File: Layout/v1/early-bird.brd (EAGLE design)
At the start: 98.5 x 80.8 mm, 61 parts, among them J1 22-27-2021-02, J2 AVR_SPI_PRG_62X3_LOCK, U1 ATMEGA328P-AU

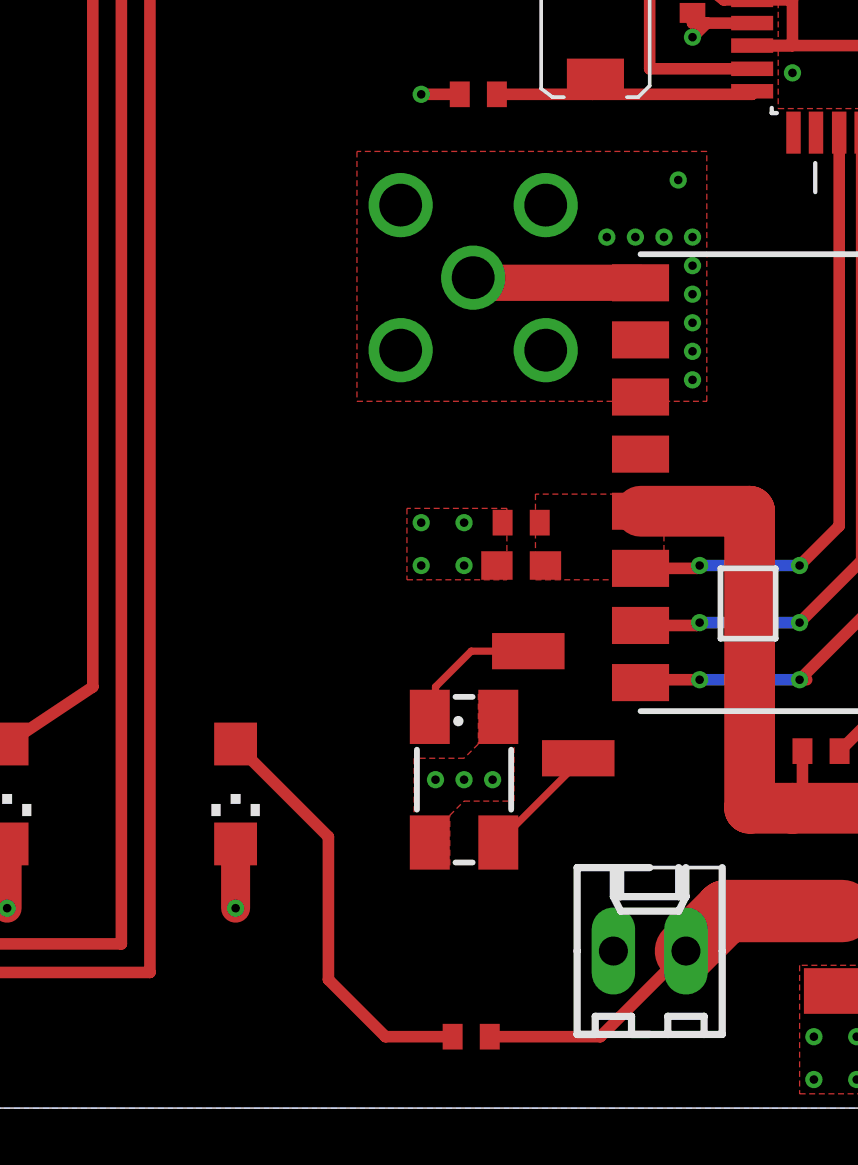
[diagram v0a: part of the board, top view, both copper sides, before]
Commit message: Update silkscreen.
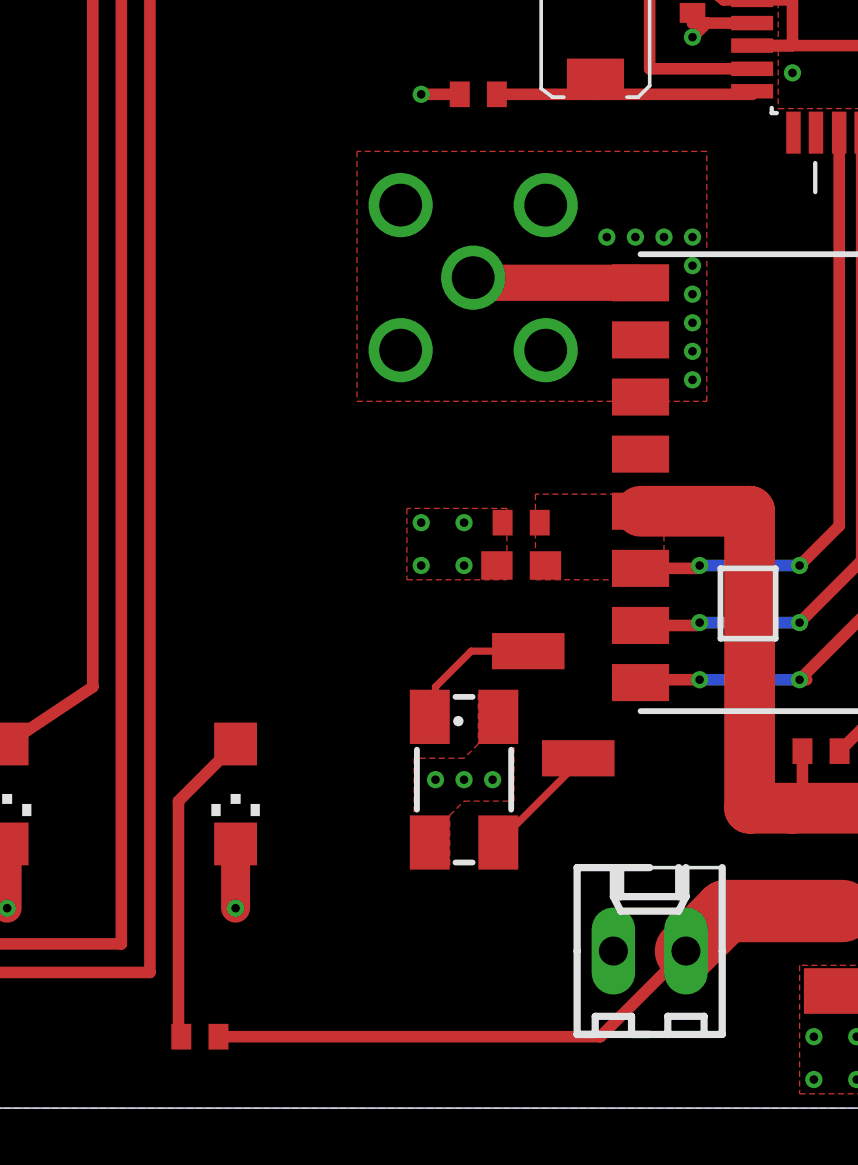
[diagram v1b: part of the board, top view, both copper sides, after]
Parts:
- moved R10 9.50 mm to (39.8, 2.50)
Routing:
- net AUX+: track 17.2 -> 26.7 mm
- net N$15: track 14.8 -> 11.2 mm
- net BATT-: vias 144 -> 143
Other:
- board text added: "10uH"
- board text added: "AA"
- board text added: "ATMega328"
- board text added: "AUX"
- board text added: "ENABLE AUX"
- board text added: "ICSP"
- board text added: "MAX-M8C"
- board text added: "RF"
- board text added: "RFM Transceiver"
- board text added: "[BGM1043N7]"
- board text removed: "L3"
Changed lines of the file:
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@@
 <text x="9.75" y="69" size="0.8128" layer="51" font="vector" ratio="15" rot="R90" align="center">1u</text>
 <text x="55.25" y="45.75" size="0.8128" layer="51" font="vector" ratio="15" rot="R180" align="center">3x 47R</text>
-<text x="49.25" y="1.5" size="0.8128" layer="51" font="vector" ratio="15" rot="R180" align="center">150R</text>
+<text x="39.75" y="1.5" size="0.8128" layer="51" font="vector" ratio="15" rot="R180" align="center">150R</text>
 <text x="2.25" y="69.75" size="0.8128" layer="51" font="vector" ratio="15" rot="R180" align="center">9.1nH</text>
 <text x="3.25" y="62.25" size="0.8128" layer="51" font="vector" ratio="15" rot="R180" align="center">8.2nH</text>
@@
 <wire x1="58.5" y1="5.5" x2="60" y2="5.5" width="0.4064" layer="51"/>
 <wire x1="59.25" y1="6.25" x2="59.25" y2="4.75" width="0.4064" layer="51"/>
-<text x="83.5" y="11" size="0.8128" layer="51" font="vector" ratio="15" rot="R90" align="center">L3</text>
+<text x="78.75" y="16.75" size="0.8128" layer="51" font="vector" ratio="15" rot="R90" align="center">10uH</text>
 <text x="51" y="38" size="0.8128" layer="51" font="vector" ratio="15" rot="R270" align="center">X1</text>
 <text x="80" y="1" size="0.8128" layer="51" font="vector" ratio="15" align="center">3n3</text>
@@
 <text x="69" y="1" size="0.8128" layer="51" font="vector" ratio="15" align="center">22K</text>
 <text x="51.5" y="14" size="0.8128" layer="51" font="vector" ratio="15" rot="R90" align="center">X2</text>
-<wire x1="51" y1="5.5" x2="52.5" y2="5.5" width="0.4064" layer="51"/>
+<text x="63.25" y="26.25" size="0.8128" layer="51" font="vector" ratio="15" rot="R180" align="center">RFM Transceiver</text>
+<text x="63.5" y="38.5" size="0.8128" layer="51" font="vector" ratio="15" rot="R180" align="center">ATMega328</text>
+<text x="15.5" y="63" size="0.8128" layer="51" font="vector" ratio="15" rot="R270" align="center">MAX-M8C</text>
+<text x="84.75" y="25.5" size="1.4224" layer="51" font="vector" ratio="15" rot="R90" align="center">ICSP</text>
+<text x="66.75" y="55.75" size="2.1844" layer="51" font="vector" ratio="15" rot="R180" align="center">AA</text>
+<text x="66.75" y="73" size="2.1844" layer="51" font="vector" ratio="15" align="center">AA</text>
+<text x="55.5" y="1.25" size="1.4224" layer="51" font="vector" ratio="15" rot="R180" align="center">AUX</text>
+<text x="55.75" y="32.25" size="1.4224" layer="51" font="vector" ratio="15" rot="R180" align="center">RF</text>
+<text x="83.75" y="10.5" size="1.4224" layer="51" font="vector" ratio="15" rot="R270" align="center">ENABLE AUX</text>
+<rectangle x1="43" y1="1" x2="52.5" y2="6.75" layer="51"/>
+<text x="5.5" y="59" size="0.8128" layer="51" font="vector" ratio="15" rot="R180" align="center">[BGM1043N7]</text>
 </plain>
 <attributes>
@@
 <attribute name="VALUE" x="38.46" y="12.27" size="1.27" layer="27" rot="R270"/>
 </element>
-<element name="R10" library="resistor" package="R0402" value="10" x="49.25" y="2.5" smashed="yes" rot="R180"/>
+<element name="R10" library="resistor" package="R0402" value="10" x="39.75" y="2.5" smashed="yes" rot="R180"/>
 <element name="C11" library="resistor" package="C0603" value="1uF" x="64.75" y="5.5" smashed="yes" rot="R270"/>
 <element name="C12" library="resistor" package="C0402" value="100n" x="66.25" y="5.5" smashed="yes" rot="R270"/>
@@
 <via x="54" y="30.5" extent="1-16" drill="0.3"/>
 <via x="56" y="30.5" extent="1-16" drill="0.3"/>
-<via x="56.5" y="32.5" extent="1-16" drill="0.3"/>
 <polygon width="0.4064" layer="1" thermals="no" rank="2">
 <vertex x="79.5" y="6.25"/>
@@
 <wire x1="68.5" y1="6" x2="67.85" y2="5.35" width="0.6096" layer="1"/>
 <wire x1="67.85" y1="5.35" x2="67.85" y2="3.25" width="0.6096" layer="1"/>
-<wire x1="53.77" y1="2.5" x2="49.9" y2="2.5" width="0.4064" layer="1"/>
+<wire x1="53.77" y1="2.5" x2="40.4" y2="2.5" width="0.4064" layer="1"/>
 <contactref element="J1" pad="1"/>
 <wire x1="53.77" y1="2.5" x2="56.77" y2="5.5" width="0.4064" layer="1"/>
@@
 <contactref element="R10" pad="2"/>
 <contactref element="LED4" pad="A"/>
-<wire x1="48.6" y1="2.5" x2="46.25" y2="2.5" width="0.4064" layer="1"/>
-<wire x1="46.25" y1="2.5" x2="44.25" y2="4.5" width="0.4064" layer="1"/>
-<wire x1="44.25" y1="4.5" x2="44.25" y2="9.5" width="0.4064" layer="1"/>
-<wire x1="44.25" y1="9.5" x2="41" y2="12.75" width="0.4064" layer="1"/>
+<wire x1="39.1" y1="2.5" x2="39" y2="2.5" width="0.4064" layer="1"/>
+<wire x1="39" y1="2.5" x2="39" y2="10.75" width="0.4064" layer="1"/>
+<wire x1="39" y1="10.75" x2="41" y2="12.75" width="0.4064" layer="1"/>
 </signal>
 <signal name="N$16">
